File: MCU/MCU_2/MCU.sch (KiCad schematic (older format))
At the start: 44 parts, among them J1 Conn_01x08, J2 Conn_01x08, J3 Conn_02x20_Odd_Even, J4 Conn_01x04, Q1 8050, U1 74HC04, U2 STM32F407VETx, Y1 12MHz

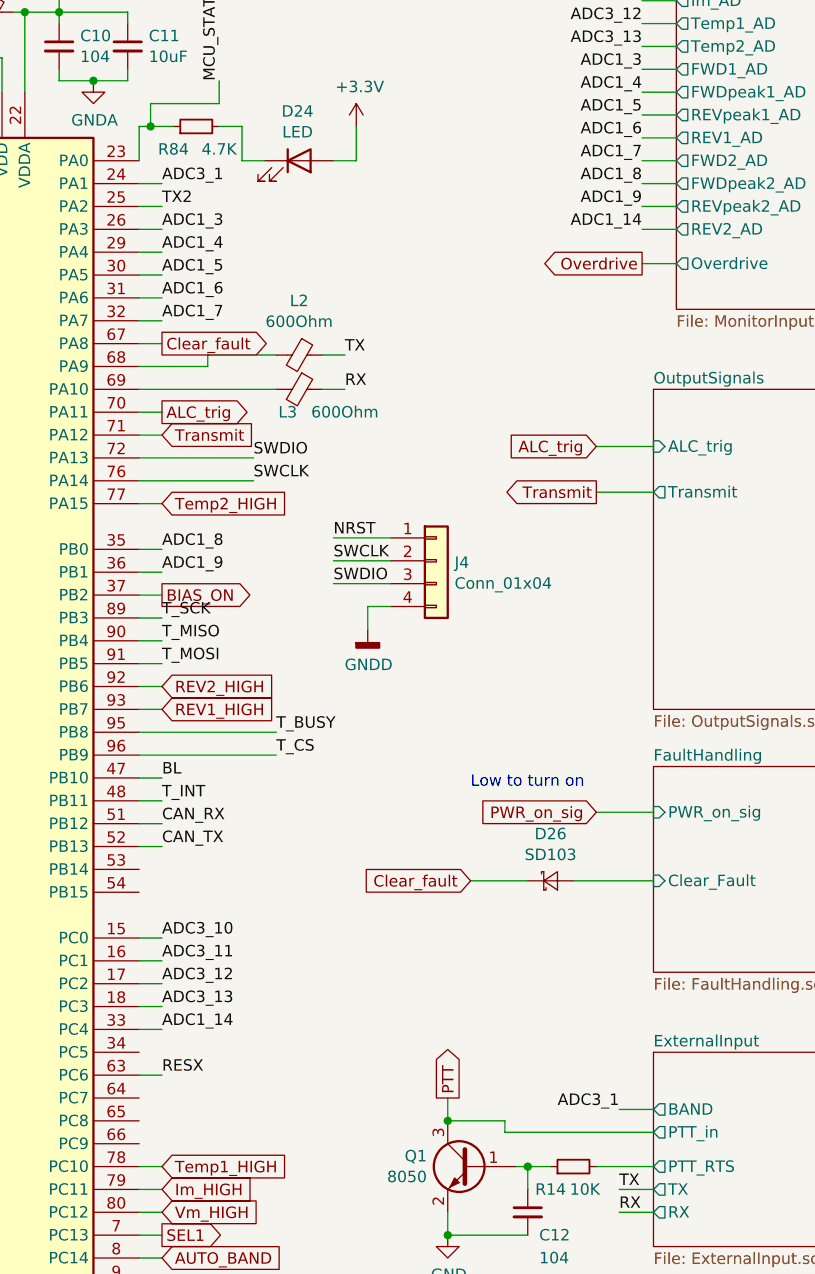
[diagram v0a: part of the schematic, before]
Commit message: OPA1000 and 2000 compatibility
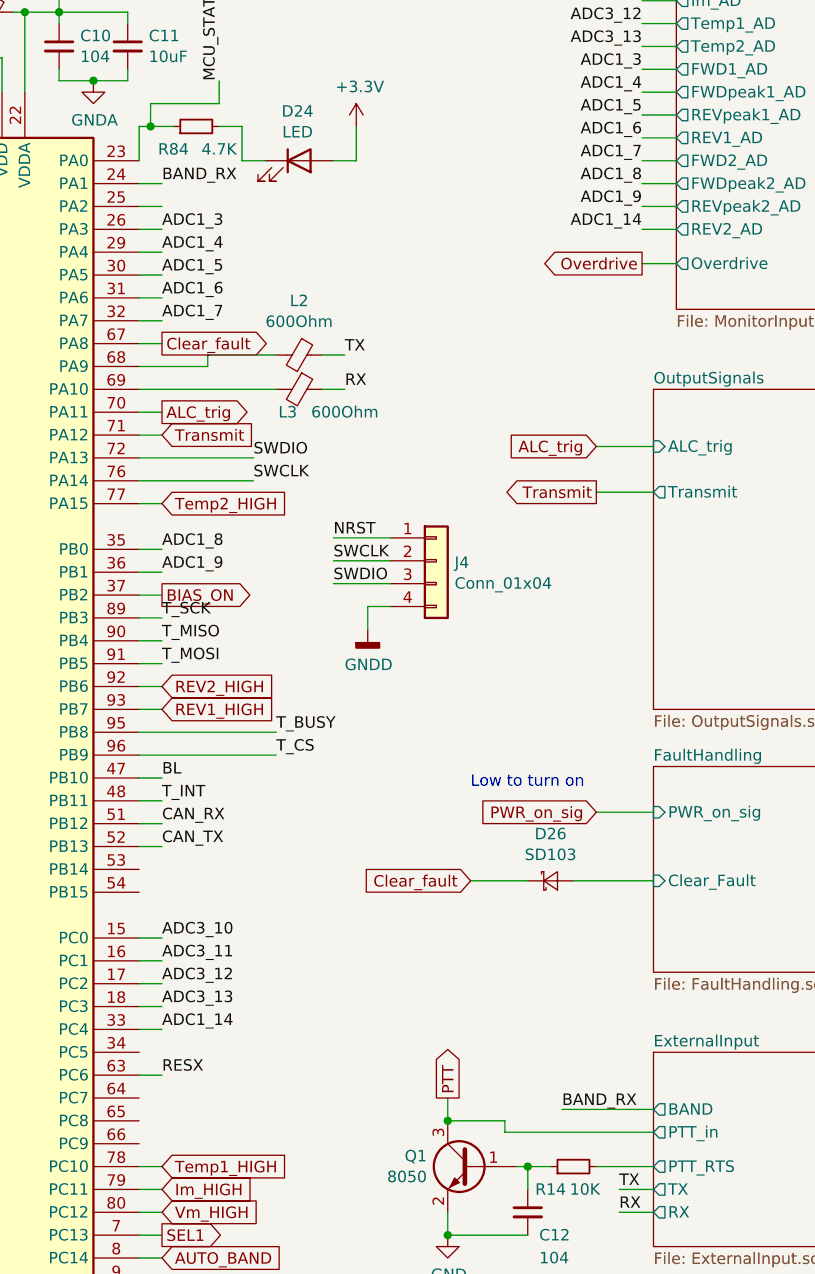
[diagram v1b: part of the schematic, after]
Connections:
- net ADC3_1 renamed BAND_RX
- net TX2: no longer names the net of U2.25 (PA2)
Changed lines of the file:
@@
 EESchema Schematic File Version 4
-LIBS:MCU-cache
 EELAYER 30 0
 EELAYER END
@@
 Wire Wire Line
 	5800 1750 5700 1750
-Text Label 5800 1650 0    50   ~ 0
-ADC3_1
 Wire Wire Line
 	5800 1650 5700 1650
@@
 Wire Wire Line
 	5800 4350 5700 4350
-Text Label 7800 5700 2    50   ~ 0
-ADC3_1
-Wire Wire Line
-	7800 5700 7950 5700
 Wire Wire Line
 	7950 5950 7700 5950
@@
 Wire Wire Line
 	3700 5550 3900 5550
-Text Label 5800 1750 0    50   ~ 0
-TX2
 Text Label 6050 1200 1    50   ~ 0
 MCU_STATE
@@
 Wire Wire Line
 	5800 3450 5700 3450
+Text Label 5800 1650 0    50   ~ 0
+BAND_RX
+Text Label 7550 5700 0    50   ~ 0
+BAND_RX
+Wire Wire Line
+	7550 5700 7950 5700
 $EndSCHEMATC
